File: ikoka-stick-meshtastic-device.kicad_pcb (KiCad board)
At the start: 2 copper layers, 100 x 28 mm, 26 parts, among them J1 Conn_Coaxial, J2 Conn_01x07_Socket, J3 Conn_01x07_Socket, J4 Conn_01x02, J5 Conn_01x02, J6 Conn_01x04, Q1 AO3401A, SW1 SW_Push, U1 MT3608, U2 E22-900M30S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

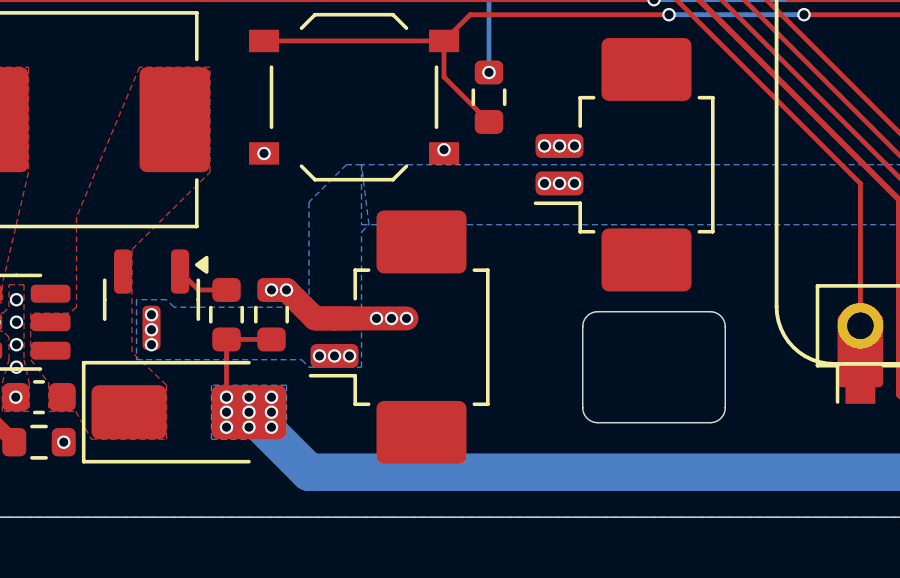
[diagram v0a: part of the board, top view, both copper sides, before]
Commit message: Update ikoka-stick-meshtastic-device.kicad_pcb
Silk screen edits to improve polarity awarness
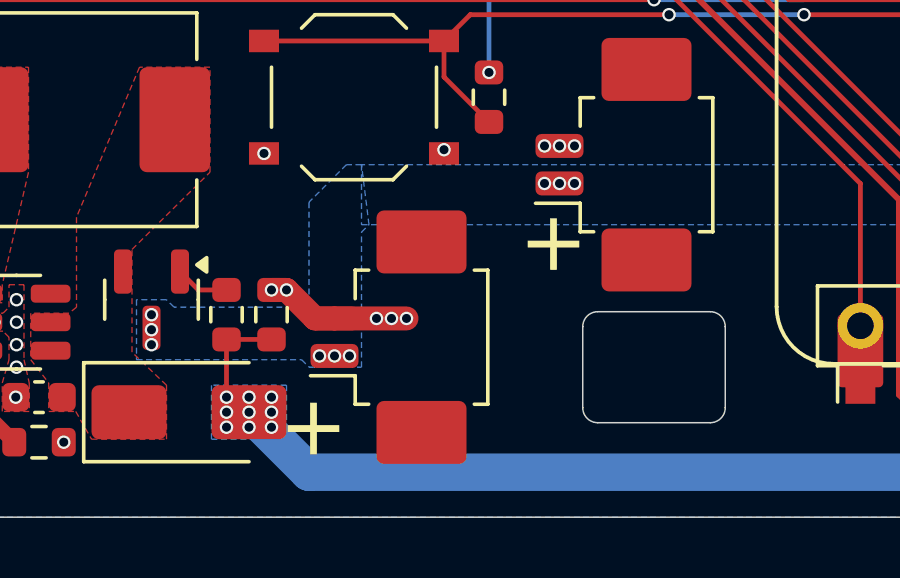
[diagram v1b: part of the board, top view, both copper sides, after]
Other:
- board text added: "+"
- board text added: "-"
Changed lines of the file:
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@@
 			(layer "B.Fab")
-		)
-		(fp_text user "+"
-			(at -43 6.25 180)
-			(layer "B.SilkS")
-			(effects
-				(font
-					(size 2 2)
-					(thickness 0.15)
-				)
-				(justify mirror)
-			)
 		)
 		(fp_text user "${REFERENCE}"
@@
 		(layer "F.SilkS")
 	)
+	(gr_text "+"
+		(at 187.5 112.15 0)
+		(layer "F.SilkS")
+		(effects
+			(font
+				(size 2 2)
+				(thickness 0.2)
+			)
+			(justify left bottom)
+		)
+	)
+	(gr_text "-"
+		(at 133 86.5 90)
+		(layer "B.SilkS")
+		(effects
+			(font
+				(size 4 4)
+				(thickness 0.4)
+			)
+			(justify left bottom mirror)
+		)
+	)
+	(gr_text "+"
+		(at 224 91.2 0)
+		(layer "B.SilkS")
+		(effects
+			(font
+				(size 4 4)
+				(thickness 0.4)
+			)
+			(justify left bottom mirror)
+		)
+	)
+	(gr_text "+"
+		(at 195.5 106 0)
+		(layer "F.SilkS")
+		(effects
+			(font
+				(size 2 2)
+				(thickness 0.2)
+			)
+			(justify left bottom)
+		)
+	)
 	(gr_poly

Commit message: pin_1_gnd
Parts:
- added REF**: SolderWirePad_1x01_SMD_1.5x3mm, Connector_Wire:SolderWirePad_1x01_SMD_1.5x3mm, F.Cu at (176.5, 95.5)
- added pin1: SolderWirePad_1x01_SMD_1.5x3mm, Connector_Wire:SolderWirePad_1x01_SMD_1.5x3mm, F.Cu at (170.7, 96.5)
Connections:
- J6 pad 1: +3V3 -> GND
- J6 pad 2: GND -> +3V3
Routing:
- net +3V3: track 59.0 -> 66.4 mm
- net GND: track 7.53 -> 13.2 mm
- net /LORA_RXEN: track 66.3 -> 67.4 mm
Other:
- board text added: "#"
- board text added: "GOME"
- board text removed: "行こか？"

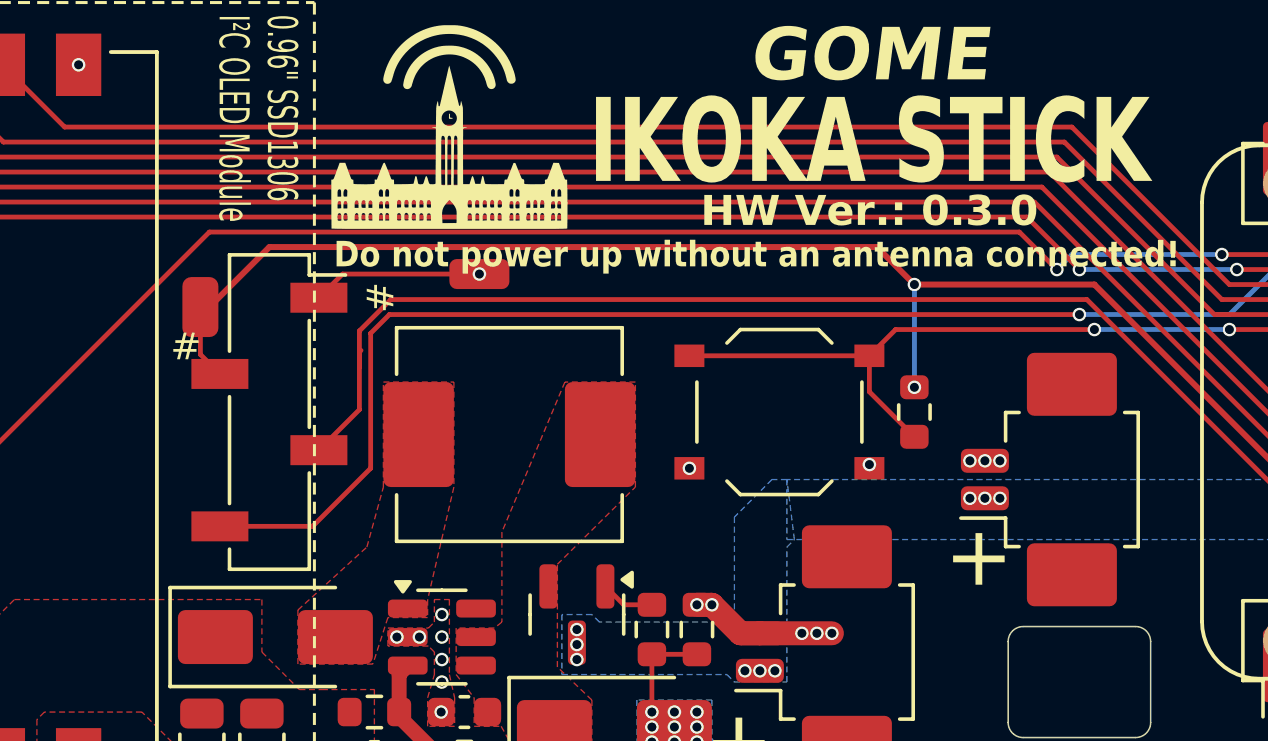
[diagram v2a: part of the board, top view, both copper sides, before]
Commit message: version update, oled pinout silk
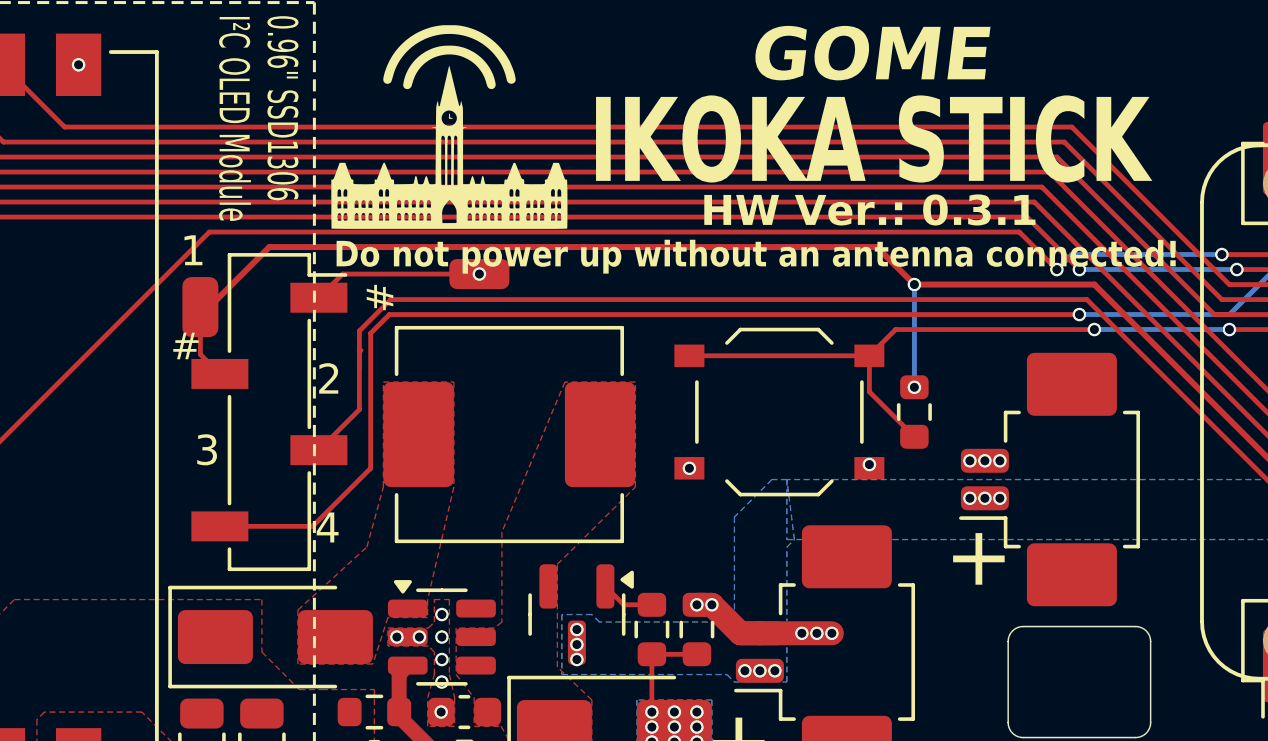
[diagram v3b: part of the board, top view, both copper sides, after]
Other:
- board text added: "+ oled 1:GND 2:3v3 3:i2c_scl 4:i2c_sda -"
- board text added: "1"
- board text added: "2"
- board text added: "3"
- board text added: "4"
- board text added: "HW Ver.: 0.3.1"
- board text removed: "HW Ver.: 0.3.0"
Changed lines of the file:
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@@
+		)
+	)
+	(gr_text "2"
+		(at 174.56 99.51 0)
+		(layer "F.SilkS")
+		(effects
+			(font
+				(size 1 1)
+				(thickness 0.1)
+			)
+			(justify left bottom)
 		)
 	)
@@
 		)
 	)
+	(gr_text "4"
+		(at 174.51 104.47 0)
+		(layer "F.SilkS")
+		(effects
+			(font
+				(size 1 1)
+				(thickness 0.1)
+			)
+			(justify left bottom)
+		)
+	)
 	(gr_text "#"
 		(at 177.24 96.7 90)
@@
 		)
 	)
+	(gr_text "1"
+		(at 170.02 95.23 0)
+		(layer "F.SilkS")
+		(effects
+			(font
+				(size 1 1)
+				(thickness 0.1)
+			)
+			(justify left bottom)
+		)
+	)
 	(gr_text "JLCJLCJLCJLC"
 		(at 158 100 0)
@@
 		)
 	)
-	(gr_text "HW Ver.: 0.3.0"
+	(gr_text "HW Ver.: 0.3.1"
 		(at 193 93.3 0)
 		(layer "F.SilkS")
@@
 			)
 		)
-		(render_cache "HW Ver.: 0.3.0" 0
+		(render_cache "HW Ver.: 0.3.1" 0
 			(polygon
 				(pts
@@
 			(polygon
 				(pts
-					(xy 198.311616 92.683653) (xy 198.376295 92.695471) (xy 198.43019 92.713787) (xy 198.480095 92.740618)
-					(xy 198.523134 92.774625) (xy 198.560005 92.816247) (xy 198.589421 92.862638) (xy 198.61367 92.917036)
-					(xy 198.632423 92.980622) (xy 198.648954 93.082274) (xy 198.654955 93.206303) (xy 198.648816 93.3307)
-					(xy 198.631691 93.435403) (xy 198.612414 93.501288) (xy 198.588141 93.555998) (xy 198.559334 93.601121)
-					(xy 198.522575 93.641412) (xy 198.479547 93.674532) (xy 198.429519 93.700833) (xy 198.375627 93.718801)
-					(xy 198.311148 93.730385) (xy 198.234185 93.734539) (xy 198.1586 93.730395) (xy 198.094237 93.718751)
-					(xy 198.039463 93.700528) (xy 197.988642 93.67387) (xy 197.945421 93.640398) (xy 197.908976 93.599778)
-					(xy 197.87923 93.553277) (xy 197.85475 93.498439) (xy 197.835886 93.433998) (xy 197.819335 93.33116)
-					(xy 197.813387 93.207646) (xy 198.077748 93.207646) (xy 198.082966 93.32896) (xy 198.096249 93.412415)
-					(xy 198.114629 93.467398) (xy 198.136752 93.503211) (xy 198.163456 93.5274) (xy 198.19538 93.541895)
-					(xy 198.234185 93.54696) (xy 198.272959 93.541897) (xy 198.304863 93.527404) (xy 198.331558 93.503215)
-					(xy 198.353681 93.467398) (xy 198.372039 93.412391) (xy 198.385333 93.328554) (xy 198.390562 93.206303)
-					(xy 198.385379 93.082511) (xy 198.372284 92.998784) (xy 198.354353 92.944841) (xy 198.332632 92.91002)
-					(xy 198.306016 92.886329) (xy 198.273785 92.872019) (xy 198.234185 92.866988) (xy 198.194553 92.872021)
-					(xy 198.162303 92.886333) (xy 198.135678 92.910024) (xy 198.113957 92.944841) (xy 198.096046 92.998809)
-					(xy 198.082941 93.082917) (xy 198.077748 93.207646) (xy 197.813387 93.207646) (xy 197.813355 93.206974)
-					(xy 197.819589 93.079391) (xy 197.836558 92.977569) (xy 197.855756 92.914248) (xy 197.880458 92.859698)
-					(xy 197.91038 92.812827) (xy 197.947251 92.772238) (xy 197.990704 92.739018) (xy 198.041539 92.71281)
-					(xy 198.09627 92.694872) (xy 198.159992 92.683457) (xy 198.234185 92.67941)
+					(xy 198.597558 93.715) (xy 197.918563 93.715) (xy 197.918563 93.539145) (xy 198.133069 93.539145)
+					(xy 198.133069 92.999856) (xy 197.918563 92.999856) (xy 197.918563 92.835725) (xy 198.01284 92.829986)
+					(xy 198.0557 92.821744) (xy 198.088006 92.810141) (xy 198.119714 92.790224) (xy 198.141251 92.76636)
+					(xy 198.154967 92.736978) (xy 198.161767 92.698949) (xy 198.387875 92.698949) (xy 198.387875 93.539145)
+					(xy 198.597558 93.539145)
 				)
 			)
@@
 			)
 			(justify left top)
+		)
+	)
+	(gr_text "3"
+		(at 170.49 101.88 0)
+		(layer "F.SilkS")
+		(effects
+			(font
+				(size 1 1)
+				(thickness 0.1)
+			)
+			(justify left bottom)
 		)
 	)
@@
 			)
 			(justify left bottom mirror)
+		)
+	)
+	(gr_text "+     oled 1:GND 2:3v3 3:i2c_scl 4:i2c_sda     -"
+		(at 210.73 100.73 0)
+		(layer "B.SilkS")
+		(effects
+			(font
+				(size 1.75 1.75)
+				(thickness 0.15)
+			)
+			(justify left bottom mirror)
